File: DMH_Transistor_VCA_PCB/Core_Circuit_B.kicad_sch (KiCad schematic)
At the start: 28 parts, among them Q1 BC548, Q2 BC548, U1 TL074

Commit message: Finished core circuit schematic
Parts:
- RV1: Function CV 1 A Amount -> CV 1 B Amount
- RV2: Function CV 2 A Amount -> CV 2 B Amount
- RV3: Function Offset A -> Offset B
- RV4: value R_Potentiometer_Trim_US -> 100k
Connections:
- net CV 1 A Input renamed CV 1 B Input
- net CV 2 A Input renamed CV 2 B Input
- net Input A renamed Input B
- net Output A renamed Output B

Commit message: Finished schematic
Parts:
- removed RV1, RV2: 100k, SynthStuff:Potentiometer_TT_P110KH1, symbol Device:R_Potentiometer_US
- renumbered Q1 to Q3, Q2 to Q4, R14 to R22, R15 to R23, R1 to R24, R18 to R25, R16 to R26, R2 to R27, R3 to R28, R20 to R29, R17 to R30, R19 to R31, R4 to R32, R11 to R33, R12 to R34, R10 to R35, R13 to R36, R5 to R37, R6 to R38, R9 to R39, R21 to R40, R8 to R41, R7 to R42, RV4 to RV6, RV3 to RV8, U1 to U2
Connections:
- net CV 1 B Pot: now reaches U2.3 (+)
- net CV 2 B Pot: now reaches U2.5 (+)

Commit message: Finished main PCB
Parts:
- removed R40: 20k, Resistor_THT:R_Axial_DIN0207_L6.3mm_D2.5mm_P7.62mm_Horizontal, symbol Device:R_US
- removed RV8: 100k, SynthStuff:Potentiometer_Alpha_RD901F-40-00D_Single_Vertical, symbol Device:R_Potentiometer_US
- Q4: footprint Package_TO_SOT_THT:TO-92_Inline -> Package_TO_SOT_THT:TO-92L_Inline_Wide
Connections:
- net Offset B Pot: now reaches R42.1

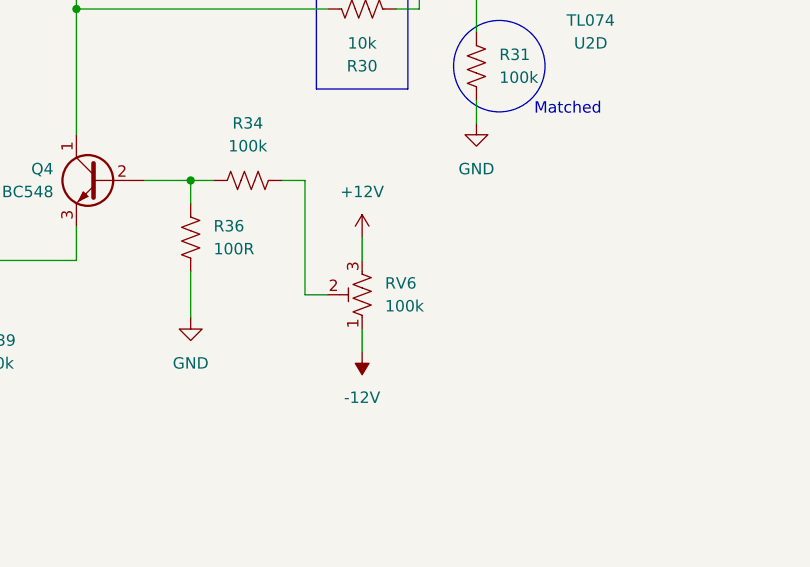
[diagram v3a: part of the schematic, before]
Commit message: Pots PCB in progress
Need to add CV input traces to the pin headers
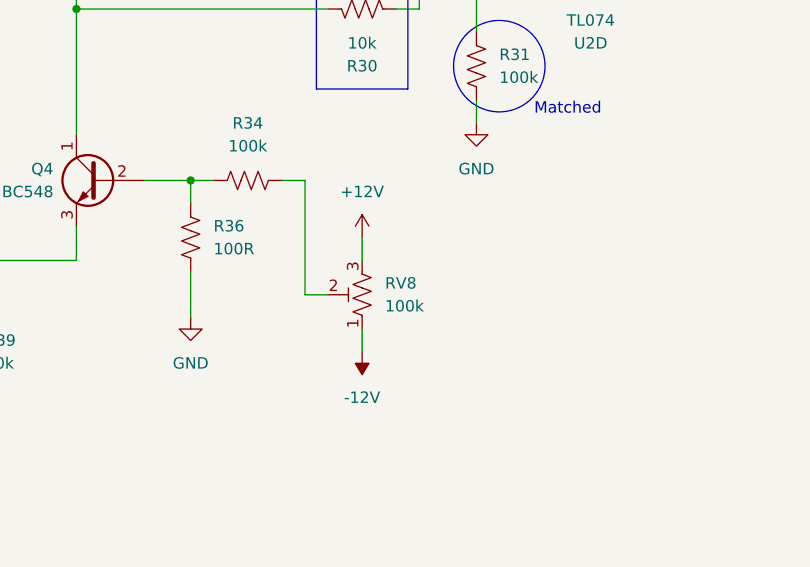
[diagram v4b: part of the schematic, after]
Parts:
- renumbered RV6 to RV8
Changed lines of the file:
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@@
 		(dnp no)
 		(fields_autoplaced yes)
-		(property "Reference" "RV6"
+		(property "Reference" "RV8"
 			(at 212.09 87.6299 0)
 			(effects
@@
 			(project "DMH_Transistor_VCA_PCB"
 				(path "/58f4306d-5387-4983-bb08-41a2313fd315/7915b580-c9b0-4472-ab9c-d9fb99b1a92f"
-					(reference "RV6")
+					(reference "RV8")
 					(unit 1)
 				)

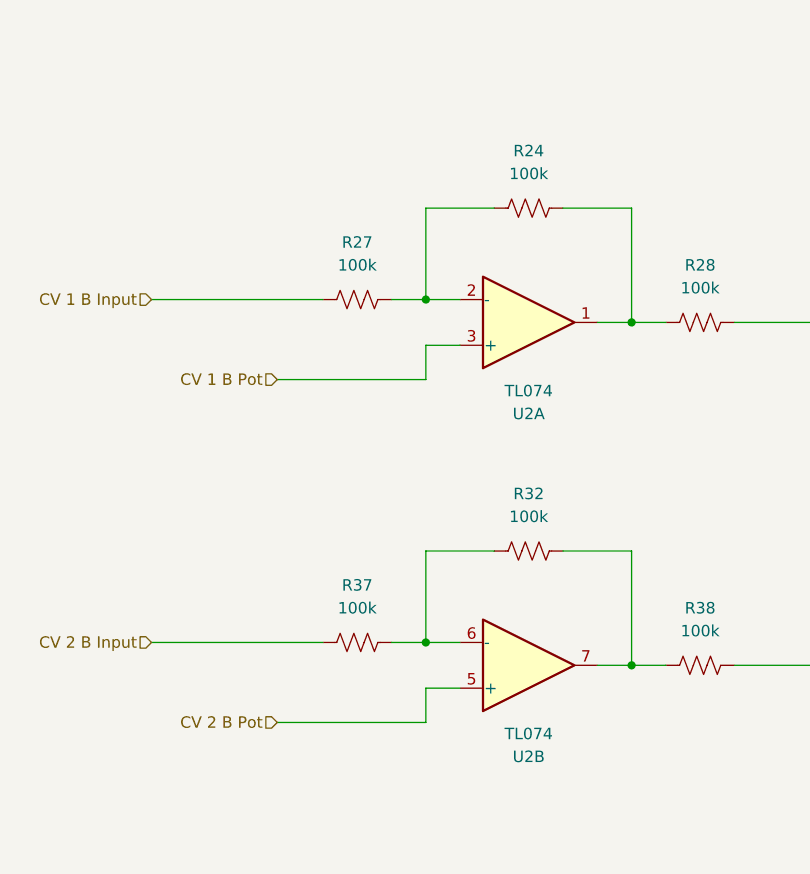
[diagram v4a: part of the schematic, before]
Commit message: Added CV input attenuverter adjustment trimpots
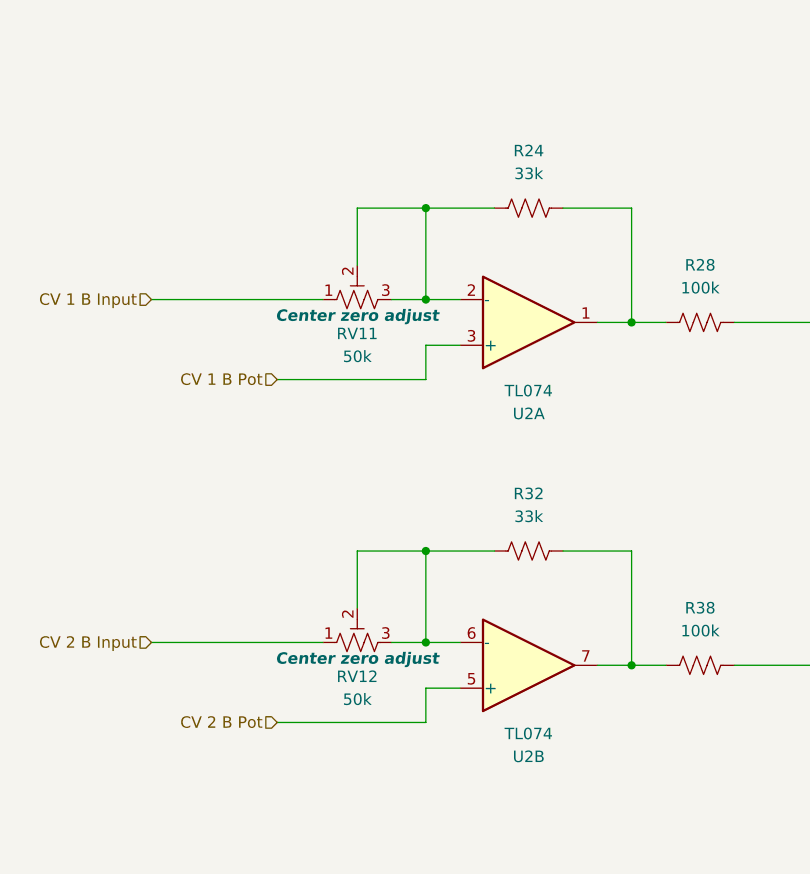
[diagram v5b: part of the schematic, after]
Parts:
- removed R27, R37: 100k, Resistor_THT:R_Axial_DIN0207_L6.3mm_D2.5mm_P7.62mm_Horizontal, symbol Device:R_US
- added RV11, RV12: 50k, Potentiometer_THT:Potentiometer_Bourns_3296W_Vertical, symbol Device:R_Potentiometer_Trim_US
- R24, R32: value 100k -> 33k
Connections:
- net CV 1 B Input: now also RV11.1
- net CV 2 B Input: now also RV12.1
- net at R24.1, U2.2 (-): now also RV11.2, RV11.3
- net at R32.1, U2.6 (-): now also RV12.2, RV12.3
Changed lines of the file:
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@@
 	)
 	(junction
+		(at 58.42 38.1)
+		(diameter 0)
+		(color 0 0 0 0)
+	)
+	(junction
 		(at 165.1 85.09)
 		(diameter 0)
@@
 	)
 	(junction
+		(at 58.42 76.2)
+		(diameter 0)
+		(color 0 0 0 0)
+	)
+	(junction
 		(at 222.25 48.26)
 		(diameter 0)
@@
 	(wire
 		(pts
+			(xy 50.8 38.1) (xy 58.42 38.1)
+		)
+		(stroke
+			(width 0)
+			(type default)
+		)
+	)
+	(wire
+		(pts
 			(xy 215.9 44.45) (xy 215.9 48.26)
 		)
@@
 	(wire
 		(pts
+			(xy 50.8 82.55) (xy 50.8 76.2)
+		)
+		(stroke
+			(width 0)
+			(type default)
+		)
+	)
+	(wire
+		(pts
 			(xy 177.8 81.28) (xy 177.8 85.09)
 		)
@@
 	(wire
 		(pts
+			(xy 50.8 44.45) (xy 50.8 38.1)
+		)
+		(stroke
+			(width 0)
+			(type default)
+		)
+	)
+	(wire
+		(pts
 			(xy 81.28 88.9) (xy 85.09 88.9)
 		)
@@
 	(wire
 		(pts
+			(xy 50.8 76.2) (xy 58.42 76.2)
+		)
+		(stroke
+			(width 0)
+			(type default)
+		)
+	)
+	(wire
+		(pts
 			(xy 92.71 88.9) (xy 101.6 88.9)
 		)
@@
 	)
 	(symbol
+		(lib_id "Device:R_Potentiometer_Trim_US")
+		(at 50.8 48.26 90)
+		(unit 1)
+		(exclude_from_sim no)
+		(in_bom yes)
+		(on_board yes)
+		(dnp no)
+		(property "Reference" "RV11"
+			(at 50.8 52.07 90)
+			(effects
+				(font
+					(size 1.27 1.27)
+				)
+			)
+		)
+		(property "Value" "50k"
+			(at 50.8 54.61 90)
+			(effects
+				(font
+					(size 1.27 1.27)
+				)
+			)
+		)
+		(property "Footprint" "Potentiometer_THT:Potentiometer_Bourns_3296W_Vertical"
+			(at 50.8 48.26 0)
+			(effects
+				(font
+					(size 1.27 1.27)
+				)
+				(hide yes)
+			)
+		)
+		(property "Datasheet" "~"
+			(at 50.8 48.26 0)
+			(effects
+				(font
+					(size 1.27 1.27)
+				)
+				(hide yes)
+			)
+		)
+		(property "Description" "Trim-potentiometer, US symbol"
+			(at 50.8 48.26 0)
+			(effects
+				(font
+					(size 1.27 1.27)
+				)
+				(hide yes)
+			)
+		)
+		(property "Function" "Center zero adjust"
+			(at 50.8 50.038 90)
+			(effects
+				(font
+					(size 1.27 1.27)
+					(thickness 0.254)
+					(bold yes)
+					(italic yes)
+				)
+			)
+		)
+		(pin "2"
+		)
+		(pin "1"
+		)
+		(pin "3"
+		)
+		(instances
+			(project "DMH_Transistor_VCA_PCB"
+				(path "/58f4306d-5387-4983-bb08-41a2313fd315/7915b580-c9b0-4472-ab9c-d9fb99b1a92f"
+					(reference "RV11")
+					(unit 1)
+				)
+			)
+		)
+	)
+	(symbol
 		(lib_id "Device:R_US")
 		(at 133.35 76.2 270)
@@
 	)
 	(symbol
+		(lib_id "Device:R_Potentiometer_Trim_US")
+		(at 50.8 86.36 90)
+		(unit 1)
+		(exclude_from_sim no)
+		(in_bom yes)
+		(on_board yes)
+		(dnp no)
+		(property "Reference" "RV12"
+			(at 50.8 90.17 90)
+			(effects
+				(font
+					(size 1.27 1.27)
+				)
+			)
+		)
+		(property "Value" "50k"
+			(at 50.8 92.71 90)
+			(effects
+				(font
+					(size 1.27 1.27)
+				)
+			)
+		)
+		(property "Footprint" "Potentiometer_THT:Potentiometer_Bourns_3296W_Vertical"
+			(at 50.8 86.36 0)
+			(effects
+				(font
+					(size 1.27 1.27)
+				)
+				(hide yes)
+			)
+		)
+		(property "Datasheet" "~"
+			(at 50.8 86.36 0)
+			(effects
+				(font
+					(size 1.27 1.27)
+				)
+				(hide yes)
+			)
+		)
+		(property "Description" "Trim-potentiometer, US symbol"
+			(at 50.8 86.36 0)
+			(effects
+				(font
+					(size 1.27 1.27)
+				)
+				(hide yes)
+			)
+		)
+		(property "Function" "Center zero adjust"
+			(at 50.8 88.138 90)
+			(effects
+				(font
+					(size 1.27 1.27)
+					(thickness 0.254)
+					(bold yes)
+					(italic yes)
+				)
+			)
+		)
+		(pin "2"
+		)
+		(pin "1"
+		)
+		(pin "3"
+		)
+		(instances
+			(project "DMH_Transistor_VCA_PCB"
+				(path "/58f4306d-5387-4983-bb08-41a2313fd315/7915b580-c9b0-4472-ab9c-d9fb99b1a92f"
+					(reference "RV12")
+					(unit 1)
+				)
+			)
+		)
+	)
+	(symbol
 		(lib_id "Device:R_US")
 		(at 165.1 95.25 180)
@@
 			)
 		)
-		(property "Value" "100k"
+		(property "Value" "33k"
 			(at 69.85 34.29 90)
 			(effects
@@
 	)
 	(symbol
-		(lib_id "Device:R_US")
-		(at 50.8 48.26 90)
-		(unit 1)
-		(exclude_from_sim no)
-		(in_bom yes)
-		(on_board yes)
-		(dnp no)
-		(fields_autoplaced yes)
-		(property "Reference" "R27"
-			(at 50.8 41.91 90)
-			(effects
-				(font
-					(size 1.27 1.27)
-				)
-			)
-		)
-		(property "Value" "100k"
-			(at 50.8 44.45 90)
-			(effects
-				(font
-					(size 1.27 1.27)
-				)
-			)
-		)
-		(property "Footprint" "Resistor_THT:R_Axial_DIN0207_L6.3mm_D2.5mm_P7.62mm_Horizontal"
-			(at 51.054 47.244 90)
-			(effects
-				(font
-					(size 1.27 1.27)
-				)
-				(hide yes)
-			)
-		)
-		(property "Datasheet" "~"
-			(at 50.8 48.26 0)
-			(effects
-				(font
-					(size 1.27 1.27)
-				)
-				(hide yes)
-			)
-		)
-		(property "Description" "Resistor, US symbol"
-			(at 50.8 48.26 0)
-			(effects
-				(font
-					(size 1.27 1.27)
-				)
-				(hide yes)
-			)
-		)
-		(pin "1"
-		)
-		(pin "2"
-		)
-		(instances
-			(project "DMH_Transistor_VCA_PCB"
-				(path "/58f4306d-5387-4983-bb08-41a2313fd315/7915b580-c9b0-4472-ab9c-d9fb99b1a92f"
-					(reference "R27")
-					(unit 1)
-				)
-			)
-		)
-	)
-	(symbol
 		(lib_id "Transistor_BJT:BC548")
 		(at 149.86 76.2 0)
@@
 	)
 	(symbol
-		(lib_id "Device:R_US")
-		(at 50.8 86.36 90)
-		(unit 1)
-		(exclude_from_sim no)
-		(in_bom yes)
-		(on_board yes)
-		(dnp no)
-		(fields_autoplaced yes)
-		(property "Reference" "R37"
-			(at 50.8 80.01 90)
-			(effects
-				(font
-					(size 1.27 1.27)
-				)
-			)
-		)
-		(property "Value" "100k"
-			(at 50.8 82.55 90)
-			(effects
-				(font
-					(size 1.27 1.27)
-				)
-			)
-		)
-		(property "Footprint" "Resistor_THT:R_Axial_DIN0207_L6.3mm_D2.5mm_P7.62mm_Horizontal"
-			(at 51.054 85.344 90)
-			(effects
-				(font
-					(size 1.27 1.27)
-				)
-				(hide yes)
-			)
-		)
-		(property "Datasheet" "~"
-			(at 50.8 86.36 0)
-			(effects
-				(font
-					(size 1.27 1.27)
-				)
-				(hide yes)
-			)
-		)
-		(property "Description" "Resistor, US symbol"
-			(at 50.8 86.36 0)
-			(effects
-				(font
-					(size 1.27 1.27)
-				)
-				(hide yes)
-			)
-		)
-		(pin "1"
-		)
-		(pin "2"
-		)
-		(instances
-			(project "DMH_Transistor_VCA_PCB"
-				(path "/58f4306d-5387-4983-bb08-41a2313fd315/7915b580-c9b0-4472-ab9c-d9fb99b1a92f"
-					(reference "R37")
-					(unit 1)
-				)
-			)
-		)
-	)
-	(symbol
 		(lib_id "power:GND")
 		(at 101.6 133.35 0)
@@
 			)
 		)
-		(property "Value" "100k"
+		(property "Value" "33k"
 			(at 69.85 72.39 90)
 			(effects

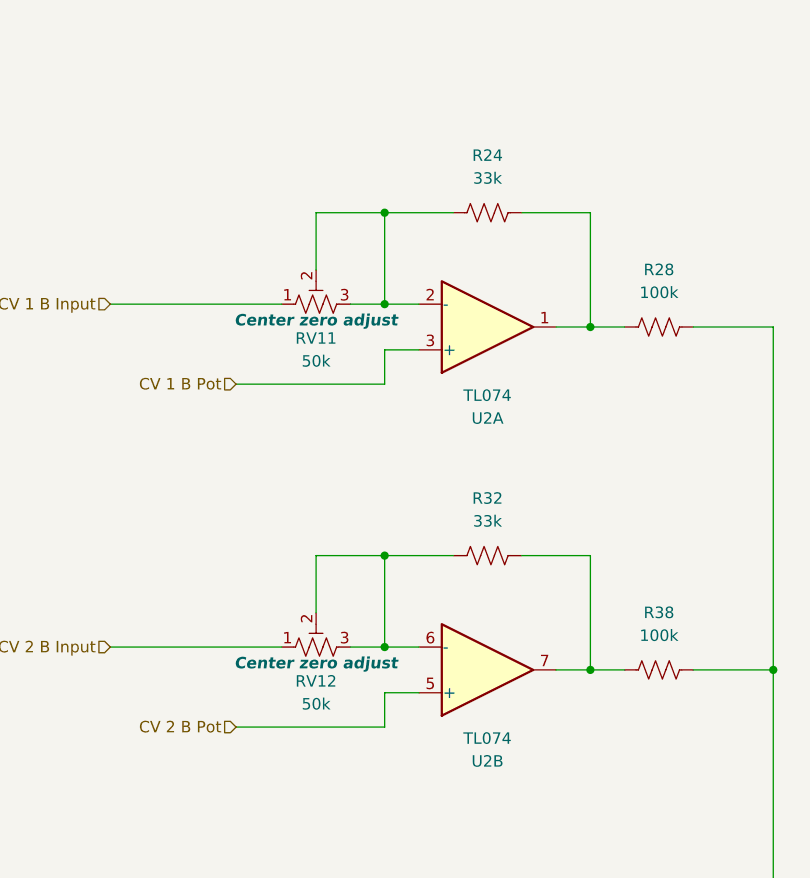
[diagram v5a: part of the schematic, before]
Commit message: Switched attenuverters trimpot and Rf positions
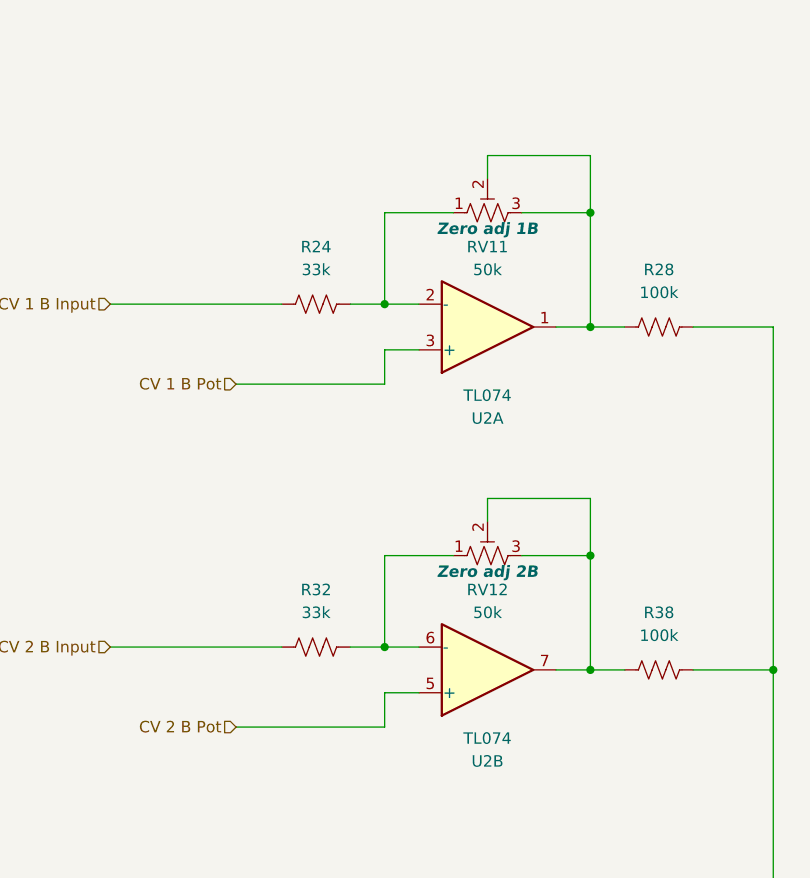
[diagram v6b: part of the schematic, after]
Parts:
- RV11: Function Center zero adjust -> Zero adj 1B
- RV12: Function Center zero adjust -> Zero adj 2B
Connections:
- net CV 1 B Input: now also R24.1; no longer RV11.1
- net CV 2 B Input: now also R32.1; no longer RV12.1
- net at RV11.2, RV11.3: now also R28.1, U2.1; no longer R24.1, U2.2 (-)
- net at R38.1, U2.7: now also RV12.2, RV12.3; no longer R32.2
- new net: R24.2, RV11.1, U2.2 (-)
- new net: R32.2, RV12.1, U2.6 (-)
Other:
- moved on the sheet: R24, R32, RV11, RV12

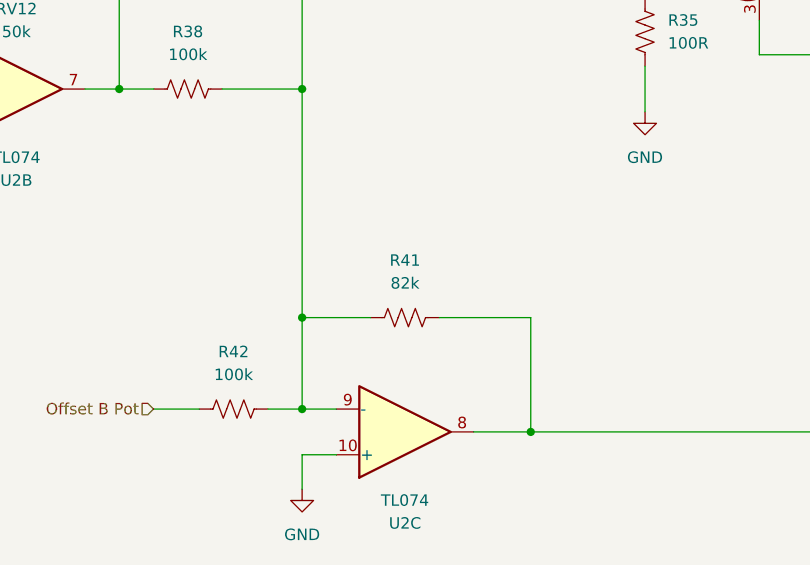
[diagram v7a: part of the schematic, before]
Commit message: Changed R8 and R41 to 100k
... in order to remove gain reduction of the incoming CV and offset
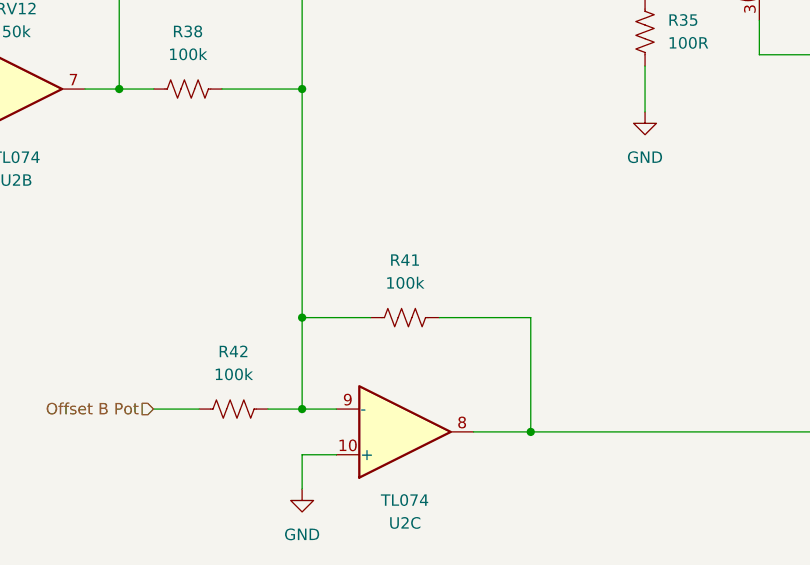
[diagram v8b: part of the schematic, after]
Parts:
- R41: value 82k -> 100k
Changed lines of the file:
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@@
 			)
 		)
-		(property "Value" "82k"
+		(property "Value" "100k"
 			(at 113.03 110.49 90)
 			(effects
